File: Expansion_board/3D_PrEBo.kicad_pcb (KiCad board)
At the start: 2 copper layers, 100 x 84 mm, 73 parts, among them J1 LED, J10 TMC_INPUT, J11 Power_out, J12 Z_Probe, J13 Fan_interconnection_header, J14 X_MIN, J15 Z_MAX, J2 V_IN, J3 RJ45, J4 X, J5 Y, J6 Z, J7 E0, J8 E1, J9 FAN&LED_INPUT, M1 Fan_3pin, M2 Fan_3pin, M3 Fan_3pin, M4 Fan_3pin, M5 Fan_3pin, M6 Fan_3pin, M7 Fan_3pin, M8 Fan_4pin, Q1 AOD4189, Q10 IRLML2502, Q2 IRLML2502, Q3 IRLML2502, Q4 IRLML2502, Q5 IRLML2502, Q6 IRLML2502, Q7 IRLML2502, Q8 IRLML2502, Q9 IRLML2502, U1 L5973D, U2 NCP1117-5.0_SOT223

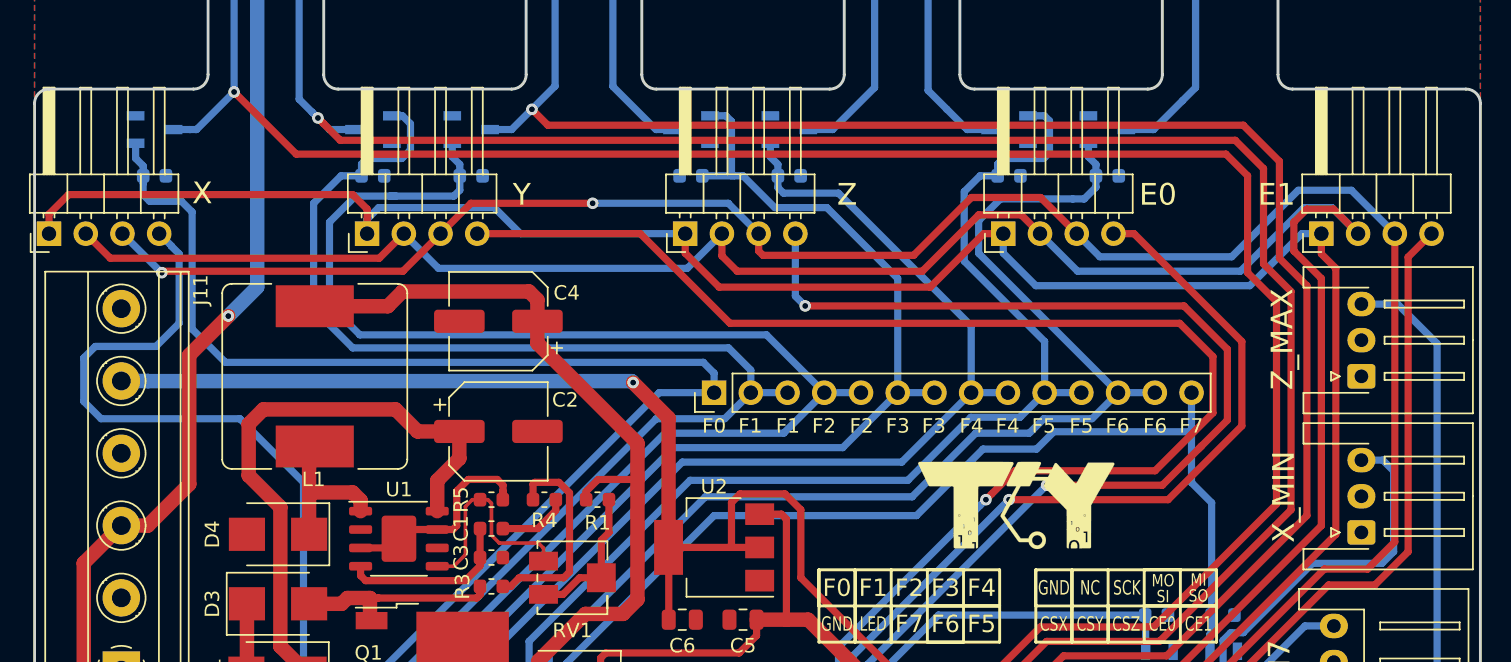
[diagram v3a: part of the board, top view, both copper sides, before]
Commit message: Expansion_board: PCB: Fix some design limitations, move endstop connector
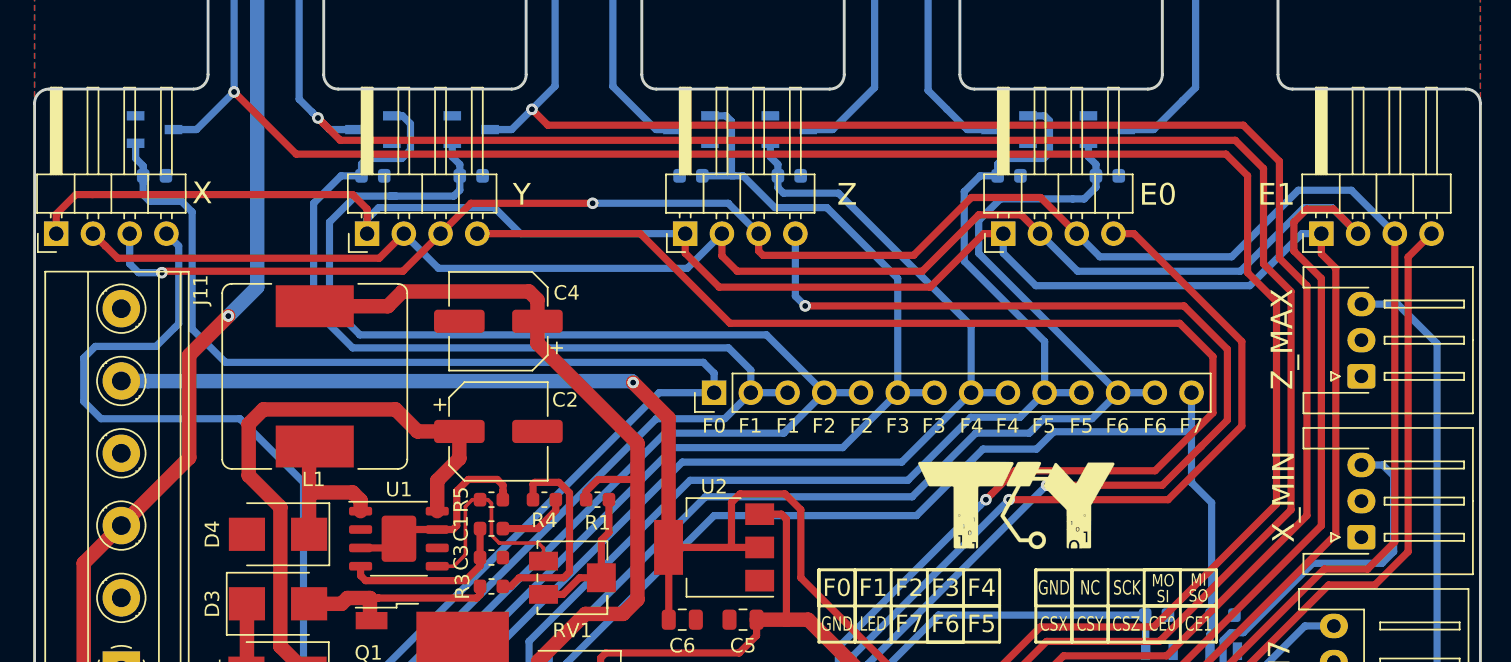
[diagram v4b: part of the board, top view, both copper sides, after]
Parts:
- moved J4 0.50 mm to (101.5, 93.0)
- moved J14 0.33 mm to (191.8, 114.0)
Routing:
- net +12V: track 318.4 -> 317.3 mm
- net MISO: track 170.1 -> 170.8 mm
- net SCK: track 176.6 -> 176.1 mm
- net MOSI: track 171.3 -> 170.8 mm
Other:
- rule via_min_size: 0.4 -> 0.6
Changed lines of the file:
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@@
     (thickness 1.6)
     (drawings 173)
-    (tracks 674)
+    (tracks 677)
     (zones 0)
     (modules 73)
@@
     (via_size 0.8)
     (via_drill 0.4)
-    (via_min_size 0.4)
+    (via_min_size 0.6)
     (via_min_drill 0.3)
     (uvia_size 0.3)
     (uvia_drill 0.1)
     (uvias_allowed no)
-    (uvia_min_size 0.2)
+    (uvia_min_size 0.3)
     (uvia_min_drill 0.1)
     (pcb_text_width 0.3)
@@
   )
   (module Connector_PinHeader_2.54mm:PinHeader_1x04_P2.54mm_Horizontal (layer F.Cu)
-    (at 101 93 90)
+    (at 101.5 93 90)
     (descr "Through hole angled pin header, 1x04, 2.54mm pitch, 6mm pin length, single row")
     (tags "Through hole angled pin header THT 1x04 2.54mm single row")
@@
   )
   (module Connector_JST:JST_XH_S03B-XH-A-1_1x03_P2.50mm_Horizontal (layer F.Cu)
-    (at 191.77 113.665 90)
+    (at 191.77 114 90)
     (descr "JST XH series connector, S03B-XH-A-1 (http://www.jst-mfg.com/product/pdf/eng/eXH.pdf), generated with kicad-footprint-generator")
     (tags "connector JST XH top entry")
@@
   (segment (start 148.7375 122) (end 149.9375 120.8) (width 0.5) (layer F.Cu) (net 6))
   (segment (start 139.15 122.35) (end 139.5 122) (width 0.5) (layer F.Cu) (net 6))
-  (segment (start 107.838477 113.19) (end 110.7 110.328477) (width 1) (layer F.Cu) (net 6))
-  (segment (start 106 113.19) (end 107.838477 113.19) (width 1) (layer F.Cu) (net 6))
   (via (at 113.4 98.7) (size 0.8) (drill 0.4) (layers F.Cu B.Cu) (net 6))
-  (segment (start 110.7 110.328477) (end 110.7 101.4) (width 1) (layer F.Cu) (net 6))
-  (segment (start 110.7 101.4) (end 113.4 98.7) (width 1) (layer F.Cu) (net 6))
   (segment (start 111.8 70.3) (end 111.8 68.58) (width 1) (layer B.Cu) (net 6))
   (segment (start 115.4 73.9) (end 111.8 70.3) (width 1) (layer B.Cu) (net 6))
@@
   (segment (start 178.8 135.4) (end 187 135.4) (width 0.5) (layer B.Cu) (net 6))
   (segment (start 174.3 130.9) (end 178.8 135.4) (width 0.5) (layer B.Cu) (net 6))
+  (segment (start 110.7 101.4) (end 113.4 98.7) (width 1) (layer F.Cu) (net 6))
+  (segment (start 106 113.19) (end 110.7 108.49) (width 1) (layer F.Cu) (net 6))
+  (segment (start 110.7 108.49) (end 110.7 101.4) (width 1) (layer F.Cu) (net 6))
   (segment (start 143.8625 114.7125) (end 143.85 114.7) (width 0.5) (layer F.Cu) (net 7))
   (segment (start 143.8625 119.7) (end 143.8625 114.7125) (width 0.5) (layer F.Cu) (net 7))
@@
   (segment (start 165.1 127) (end 165.1 128.06066) (width 0.5) (layer B.Cu) (net 19))
   (segment (start 165.1 128.06066) (end 166.13934 129.1) (width 0.5) (layer B.Cu) (net 19))
-  (segment (start 194 109.42) (end 193.245 108.665) (width 0.5) (layer B.Cu) (net 20))
   (segment (start 188.4 115.8) (end 193.2 115.8) (width 0.5) (layer B.Cu) (net 20))
-  (segment (start 193.245 108.665) (end 191.77 108.665) (width 0.5) (layer B.Cu) (net 20))
   (segment (start 183.6 120.6) (end 188.4 115.8) (width 0.5) (layer B.Cu) (net 20))
   (segment (start 182.729998 120.6) (end 183.6 120.6) (width 0.5) (layer B.Cu) (net 20))
   (segment (start 171.24066 127) (end 175.04066 123.2) (width 0.5) (layer B.Cu) (net 20))
-  (segment (start 194 115) (end 194 109.42) (width 0.5) (layer B.Cu) (net 20))
   (segment (start 193.2 115.8) (end 194 115) (width 0.5) (layer B.Cu) (net 20))
   (segment (start 170.18 127) (end 171.24066 127) (width 0.5) (layer B.Cu) (net 20))
@@
   (segment (start 182.2 122.8) (end 182.2 121.129998) (width 0.5) (layer B.Cu) (net 20))
   (segment (start 182.2 121.129998) (end 182.729998 120.6) (width 0.5) (layer B.Cu) (net 20))
+  (segment (start 194 109.755) (end 194 110.75) (width 0.5) (layer B.Cu) (net 20))
+  (segment (start 193.245 109) (end 194 109.755) (width 0.5) (layer B.Cu) (net 20))
+  (segment (start 191.77 109) (end 193.245 109) (width 0.5) (layer B.Cu) (net 20))
+  (segment (start 194 115) (end 194 110.75) (width 0.5) (layer B.Cu) (net 20))
   (segment (start 123 91.3) (end 123 93) (width 0.5) (layer F.Cu) (net 21))
   (segment (start 122 90.3) (end 123 91.3) (width 0.5) (layer F.Cu) (net 21))
-  (segment (start 102.35 90.3) (end 122 90.3) (width 0.5) (layer F.Cu) (net 21))
-  (segment (start 101 93) (end 101 91.65) (width 0.5) (layer F.Cu) (net 21))
-  (segment (start 101 91.65) (end 102.35 90.3) (width 0.5) (layer F.Cu) (net 21))
   (segment (start 133.6 93) (end 145 93) (width 0.5) (layer B.Cu) (net 21))
   (segment (start 131.8 91.2) (end 133.6 93) (width 0.5) (layer B.Cu) (net 21))
@@
   (segment (start 184.05 96.6) (end 169.25 96.6) (width 0.5) (layer B.Cu) (net 21))
   (segment (start 187.65 93) (end 184.05 96.6) (width 0.5) (layer B.Cu) (net 21))
+  (segment (start 102.85 90.3) (end 104 90.3) (width 0.5) (layer F.Cu) (net 21))
+  (segment (start 101.5 91.65) (end 102.85 90.3) (width 0.5) (layer F.Cu) (net 21))
+  (segment (start 101.5 93) (end 101.5 91.65) (width 0.5) (layer F.Cu) (net 21))
+  (segment (start 104 90.3) (end 122 90.3) (width 0.5) (layer F.Cu) (net 21))
   (segment (start 147.54 93) (end 145.14 95.4) (width 0.5) (layer B.Cu) (net 22))
   (segment (start 127.94 95.4) (end 125.54 93) (width 0.5) (layer B.Cu) (net 22))
   (segment (start 145.14 95.4) (end 127.94 95.4) (width 0.5) (layer B.Cu) (net 22))
   (segment (start 123.84 94.7) (end 125.54 93) (width 0.5) (layer F.Cu) (net 22))
-  (segment (start 103.54 93) (end 105.24 94.7) (width 0.5) (layer F.Cu) (net 22))
-  (segment (start 105.24 94.7) (end 123.84 94.7) (width 0.5) (layer F.Cu) (net 22))
   (segment (start 155 125.6) (end 150.625 125.6) (width 0.5) (layer F.Cu) (net 22))
   (segment (start 158.4 129) (end 155 125.6) (width 0.5) (layer F.Cu) (net 22))
@@
   (segment (start 169.54 93) (end 172.14 95.6) (width 0.5) (layer B.Cu) (net 22))
   (segment (start 172.14 95.6) (end 183.4 95.6) (width 0.5) (layer B.Cu) (net 22))
+  (segment (start 104.899999 93.849999) (end 105.75 94.7) (width 0.5) (layer F.Cu) (net 22))
+  (segment (start 104.889999 93.849999) (end 104.899999 93.849999) (width 0.5) (layer F.Cu) (net 22))
+  (segment (start 104.04 93) (end 104.889999 93.849999) (width 0.5) (layer F.Cu) (net 22))
+  (segment (start 105.75 94.7) (end 123.84 94.7) (width 0.5) (layer F.Cu) (net 22))
   (segment (start 150.08 93) (end 147.98 90.9) (width 0.5) (layer B.Cu) (net 23))
   (segment (start 147.98 90.9) (end 138.6 90.9) (width 0.5) (layer B.Cu) (net 23))
@@
   (segment (start 128.08 93) (end 125.48 95.6) (width 0.5) (layer F.Cu) (net 23))
   (segment (start 125.48 95.6) (end 108.9 95.6) (width 0.5) (layer F.Cu) (net 23))
-  (segment (start 108.78 95.7) (end 106.08 93) (width 0.5) (layer B.Cu) (net 23))
-  (segment (start 108.8 95.7) (end 108.78 95.7) (width 0.5) (layer B.Cu) (net 23))
   (segment (start 194.08 114.32) (end 194.08 93) (width 0.5) (layer F.Cu) (net 23))
   (segment (start 157.0286 130.9) (end 174.5 130.9) (width 0.5) (layer F.Cu) (net 23))
@@
   (segment (start 191.08 90) (end 194.08 93) (width 0.5) (layer B.Cu) (net 23))
   (segment (start 173.68 94.6) (end 182.8 94.6) (width 0.5) (layer B.Cu) (net 23))
-  (segment (start 109.469999 93.849999) (end 109.469999 93.869999) (width 0.5) (layer B.Cu) (net 24))
-  (segment (start 108.62 93) (end 109.469999 93.849999) (width 0.5) (layer B.Cu) (net 24))
-  (segment (start 109.469999 93.869999) (end 110 94.4) (width 0.5) (layer B.Cu) (net 24))
-  (segment (start 110 94.4) (end 110 99.2) (width 0.5) (layer B.Cu) (net 24))
-  (segment (start 110 99.2) (end 108.4 100.8) (width 0.5) (layer B.Cu) (net 24))
+  (segment (start 108.8 95.7) (end 107.2 95.7) (width 0.5) (layer B.Cu) (net 23))
+  (segment (start 106.58 95.08) (end 106.58 93) (width 0.5) (layer B.Cu) (net 23))
+  (segment (start 107.2 95.7) (end 106.58 95.08) (width 0.5) (layer B.Cu) (net 23))
   (segment (start 108.4 100.8) (end 104.2 100.8) (width 0.5) (layer B.Cu) (net 24))
   (segment (start 104.2 100.8) (end 103.4 101.6) (width 0.5) (layer B.Cu) (net 24))
@@
   (via (at 121.3 137.3) (size 0.8) (drill 0.4) (layers F.Cu B.Cu) (net 24))
   (segment (start 120.2 136.2) (end 121.3 137.3) (width 0.5) (layer B.Cu) (net 24))
+  (segment (start 109.969999 99.230001) (end 109.7 99.5) (width 0.5) (layer B.Cu) (net 24))
+  (segment (start 109.969999 93.849999) (end 109.969999 99.230001) (width 0.5) (layer B.Cu) (net 24))
+  (segment (start 109.12 93) (end 109.969999 93.849999) (width 0.5) (layer B.Cu) (net 24))
+  (segment (start 109.7 99.5) (end 108.4 100.8) (width 0.5) (layer B.Cu) (net 24))
   (segment (start 145.415 130.81) (end 146.625 129.6) (width 0.25) (layer B.Cu) (net 25))
   (segment (start 146.625 129.6) (end 154.4 129.6) (width 0.25) (layer B.Cu) (net 25))

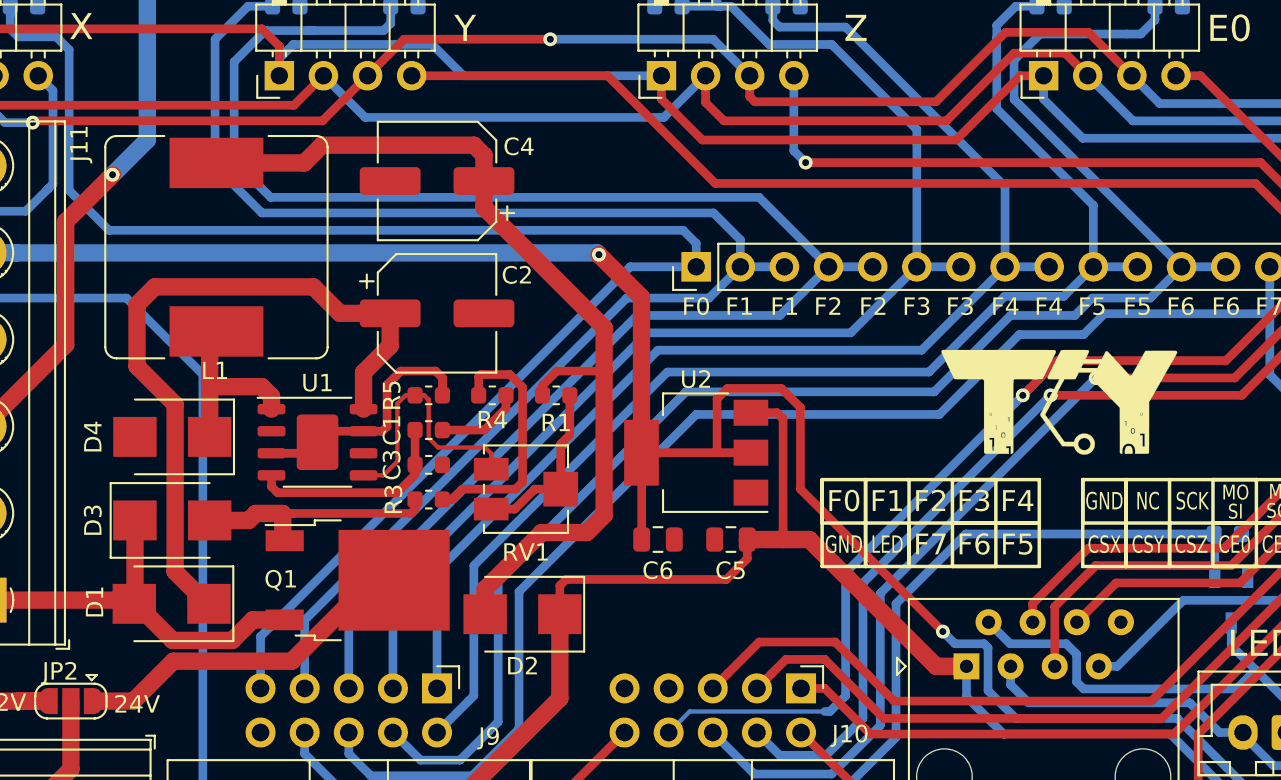
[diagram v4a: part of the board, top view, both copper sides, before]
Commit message: Expansion_board: PCB: Add trnasil, reroute capacitors
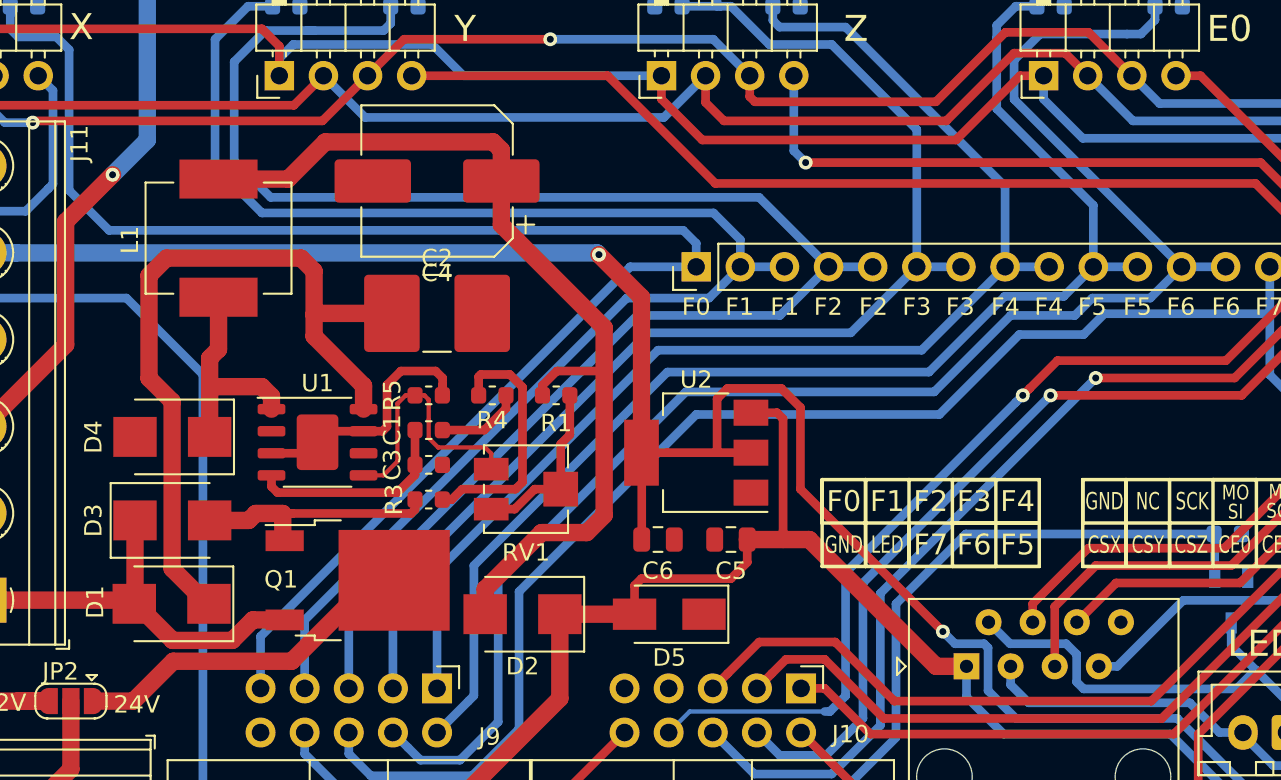
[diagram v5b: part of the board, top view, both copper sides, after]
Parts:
- removed G***: LOGO, TCY_logo:TCY_LOGO_13x6mm
- added D5: D_TVS_ALT, Diode_SMD:D_SMA, F.Cu at (145.4, 124.0)
- C2: value 100uF 35V -> 10uF 35V; footprint Capacitor_SMD:CP_Elec_6.3x7.7 -> Capacitor_SMD:C_2816_7142Metric_Pad3.20x4.45mm_HandSolder
- C4: value 300uF 6.3V -> 300uF 16V; footprint Capacitor_SMD:CP_Elec_6.3x7.7 -> Capacitor_SMD:CP_Elec_8x10.5
- L1: footprint Inductor_SMD:L_Bourns_SRR1260 -> Inductor_SMD:L_Neosid_Ms85
- moved L1 0.53 mm to (119.5, 102.3)
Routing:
- net Net-(C2-Pad1): track 40.8 -> 44.2 mm
- net Net-(D4-Pad1): track 10.8 -> 12.8 mm
- net Net-(C4-Pad1): track 54.2 -> 55.4 mm

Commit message: Expansion_board: PCB: Update logo position
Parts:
- added G***: LOGO, TCY_logo:TCY_LOGO_13x6mm, F.Cu at (168.0, 111.5)
